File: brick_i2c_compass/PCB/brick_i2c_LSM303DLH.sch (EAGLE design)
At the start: 10 parts, among them J1 BRICK_I2C

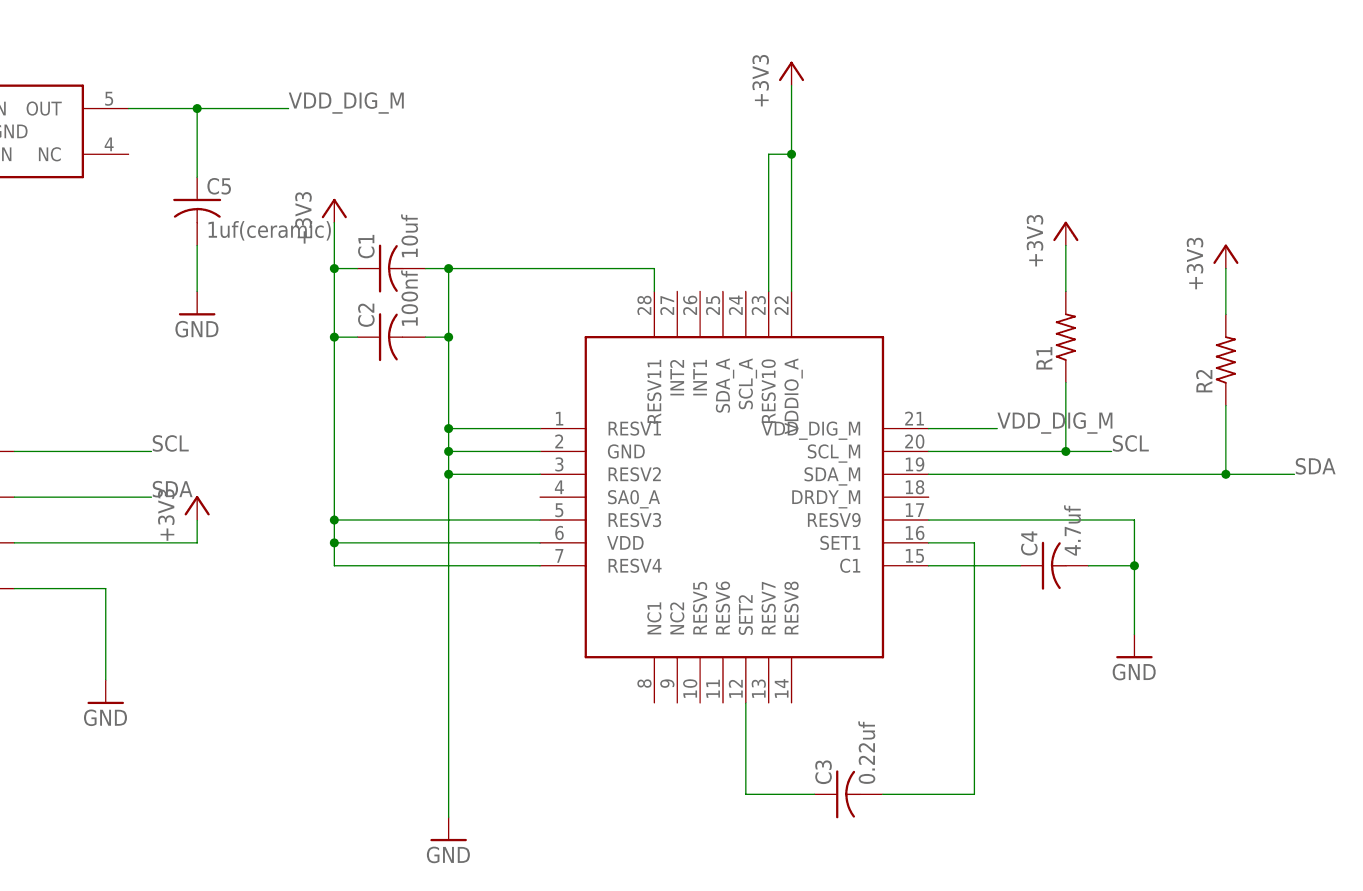
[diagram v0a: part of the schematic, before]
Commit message: Modified for Elecrow
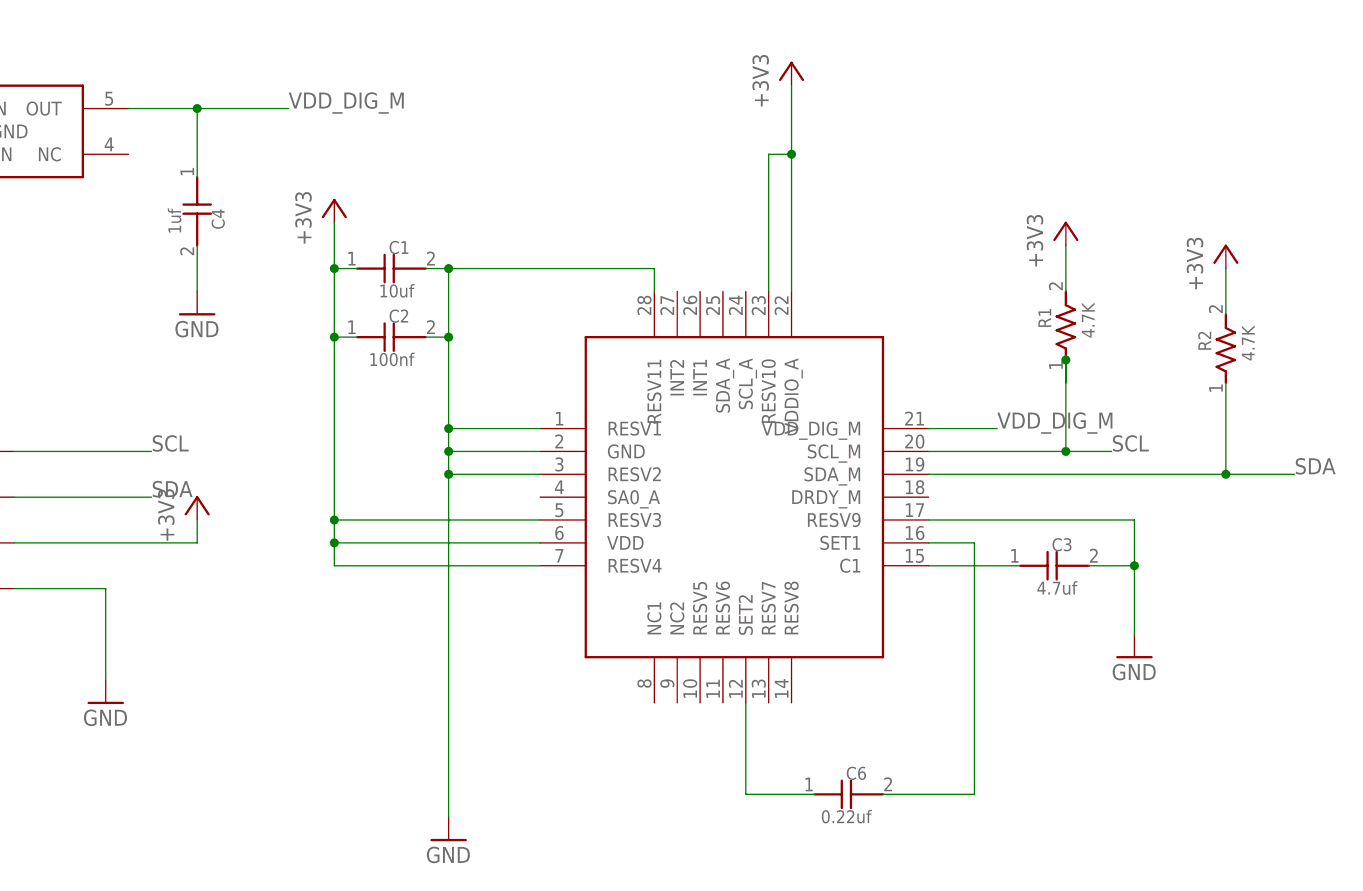
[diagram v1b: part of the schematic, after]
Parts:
- removed C5: 1uf(ceramic), adafruit:C-USC0603
- added C6: 0.22uf, GClue-Capacitor:CAPACITOR0603
- C1, C2: device adafruit:C-USC0603 -> GClue-Capacitor:CAPACITOR0603
- C3: value 0.22uf -> 4.7uf; device adafruit:C-USC0603 -> GClue-Capacitor:CAPACITOR0603
- C4: value 4.7uf -> 1uf; device adafruit:C-USC0603 -> GClue-Capacitor:CAPACITOR0603
- R1, R2: value (none) -> 4.7K; device adafruit:R-US_R0603 -> GClue-Resistors:RESISTOR0603
- U$2: device gclueSensor:ST-LSM303DLH -> GClue-Mems:ST-LSM303DLH
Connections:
- net GND: now also C3.2; no longer C5.2
- net N$1: now also C6.1; no longer C3.1
- net N$2: now also C6.2; no longer C3.2
- net N$3: now also C3.1; no longer C4.1
- net VDD_DIG_M: now also C4.1; no longer C5.1
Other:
- moved on the sheet: R1, R2

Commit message: Update for elecrow
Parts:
- added U$4: (no value), gclue:LOGO_GCLUE-M
- added U$5: (no value), gclue:LOGO_OSHW_T-M
- J1: value BRICK_I2C -> (none)
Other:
- moved on the sheet: J1
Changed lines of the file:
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@@
 <parts>
 <part name="U$1" library="gclue" deviceset="A4L-LOC" device=""/>
-<part name="J1" library="gclue" deviceset="BRICK_I2C" device=""/>
 <part name="GND1" library="supply1" deviceset="GND" device=""/>
 <part name="GND2" library="supply1" deviceset="GND" device=""/>
@@
 <part name="C3" library="GClue-Capacitor" deviceset="CAPACITOR" device="0603" value="4.7uf"/>
 <part name="C4" library="GClue-Capacitor" deviceset="CAPACITOR" device="0603" value="1uf"/>
+<part name="J1" library="gclue" deviceset="BRICK_I2C" device=""/>
+<part name="U$4" library="gclue" deviceset="LOGO_GCLUE" device="-M"/>
+<part name="U$5" library="gclue" deviceset="LOGO_OSHW_T" device="-M"/>
 </parts>
 <sheets>
@@
 <instances>
 <instance part="U$1" gate="G$1" x="0" y="0"/>
-<instance part="J1" gate="G$1" x="40.64" y="63.5"/>
 <instance part="GND1" gate="1" x="58.42" y="43.18"/>
 <instance part="GND2" gate="1" x="96.52" y="27.94"/>
@@
 <instance part="C3" gate="G$1" x="162.56" y="58.42"/>
 <instance part="C4" gate="G$1" x="68.58" y="99.06" rot="R270"/>
+<instance part="J1" gate="G$1" x="35.56" y="63.5"/>
+<instance part="U$4" gate="G$1" x="182.88" y="7.62"/>
+<instance part="U$5" gate="G$1" x="200.66" y="12.7"/>
 </instances>
 <busses>
@@
 <net name="GND" class="0">
 <segment>
-<pinref part="J1" gate="G$1" pin="GND"/>
-<wire x1="48.26" y1="55.88" x2="58.42" y2="55.88" width="0.1524" layer="91"/>
+<wire x1="43.18" y1="55.88" x2="58.42" y2="55.88" width="0.1524" layer="91"/>
 <wire x1="58.42" y1="55.88" x2="58.42" y2="45.72" width="0.1524" layer="91"/>
 <pinref part="GND1" gate="1" pin="GND"/>
+<pinref part="J1" gate="G$1" pin="GND"/>
 </segment>
 <segment>
@@
 <net name="+3V3" class="0">
 <segment>
+<pinref part="+3V1" gate="G$1" pin="+3V3"/>
+<wire x1="43.18" y1="60.96" x2="68.58" y2="60.96" width="0.1524" layer="91"/>
+<wire x1="68.58" y1="60.96" x2="68.58" y2="63.5" width="0.1524" layer="91"/>
 <pinref part="J1" gate="G$1" pin="VCC"/>
-<pinref part="+3V1" gate="G$1" pin="+3V3"/>
-<wire x1="48.26" y1="60.96" x2="68.58" y2="60.96" width="0.1524" layer="91"/>
-<wire x1="68.58" y1="60.96" x2="68.58" y2="63.5" width="0.1524" layer="91"/>
 </segment>
 <segment>
@@
 </segment>
 <segment>
+<wire x1="43.18" y1="66.04" x2="63.5" y2="66.04" width="0.1524" layer="91"/>
+<label x="63.5" y="66.04" size="1.778" layer="95"/>
 <pinref part="J1" gate="G$1" pin="SDA"/>
-<wire x1="48.26" y1="66.04" x2="63.5" y2="66.04" width="0.1524" layer="91"/>
-<label x="63.5" y="66.04" size="1.778" layer="95"/>
 </segment>
 </net>
@@
 </segment>
 <segment>
+<wire x1="43.18" y1="71.12" x2="63.5" y2="71.12" width="0.1524" layer="91"/>
+<label x="63.5" y="71.12" size="1.778" layer="95"/>
 <pinref part="J1" gate="G$1" pin="SCL"/>
-<wire x1="48.26" y1="71.12" x2="63.5" y2="71.12" width="0.1524" layer="91"/>
-<label x="63.5" y="71.12" size="1.778" layer="95"/>
-</segment>
-</net>
+</segment>
+</net>

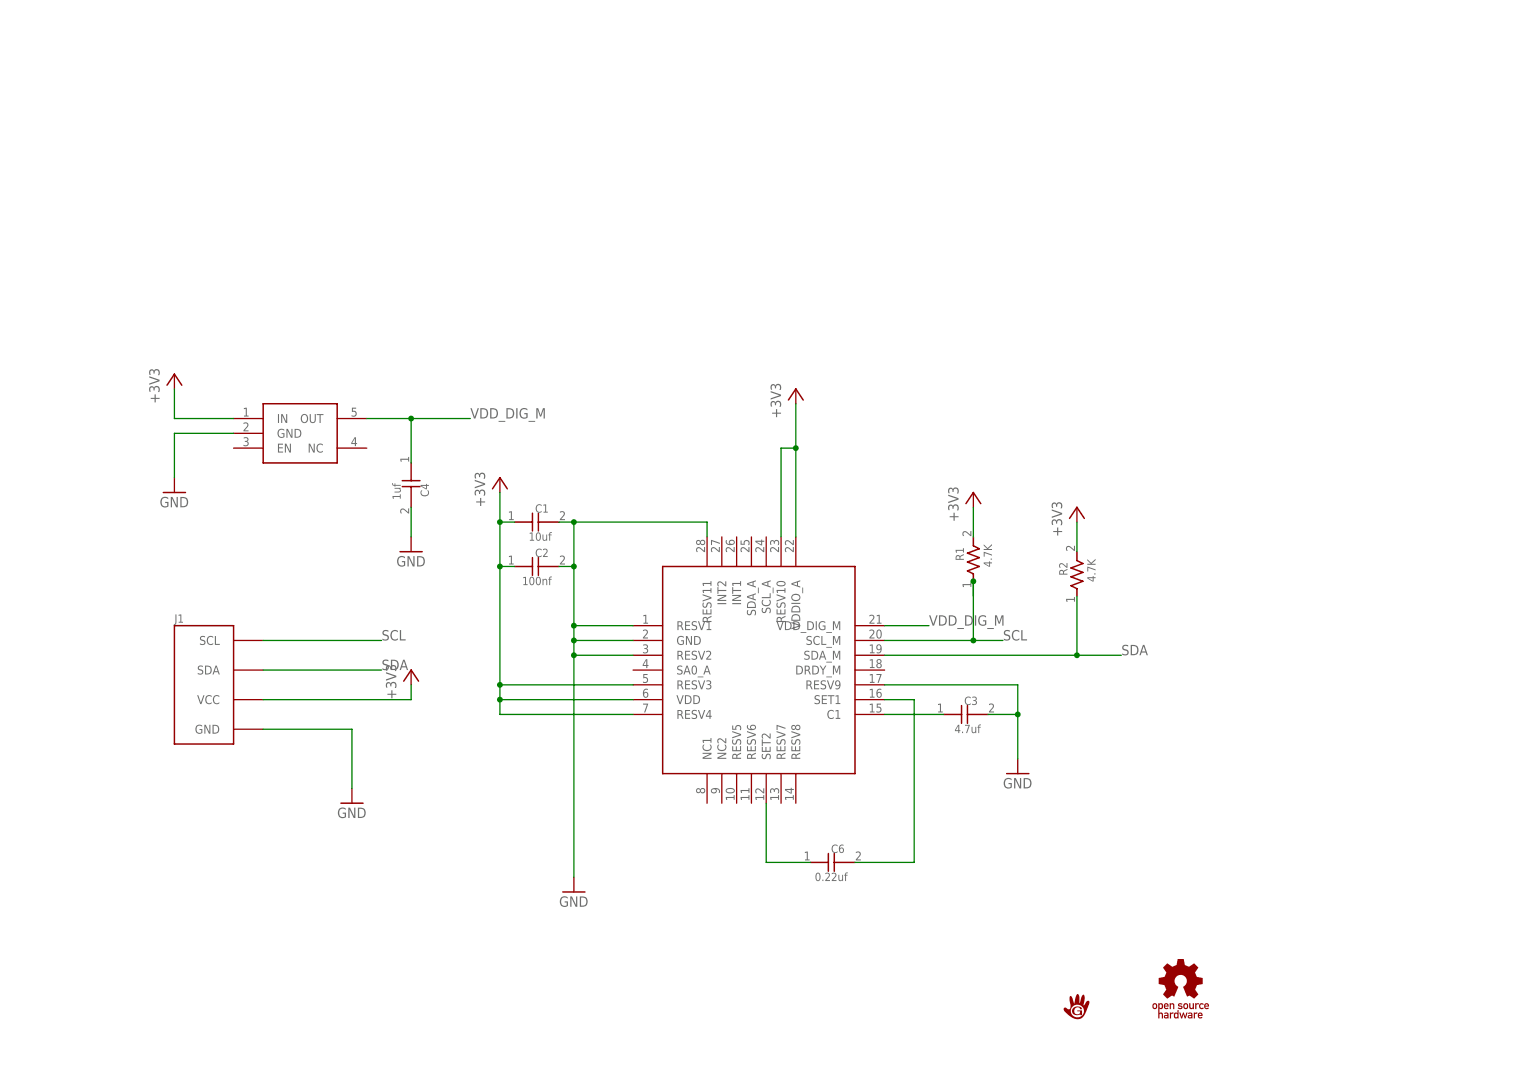
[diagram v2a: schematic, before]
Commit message: refine board size brick_i2c_compass
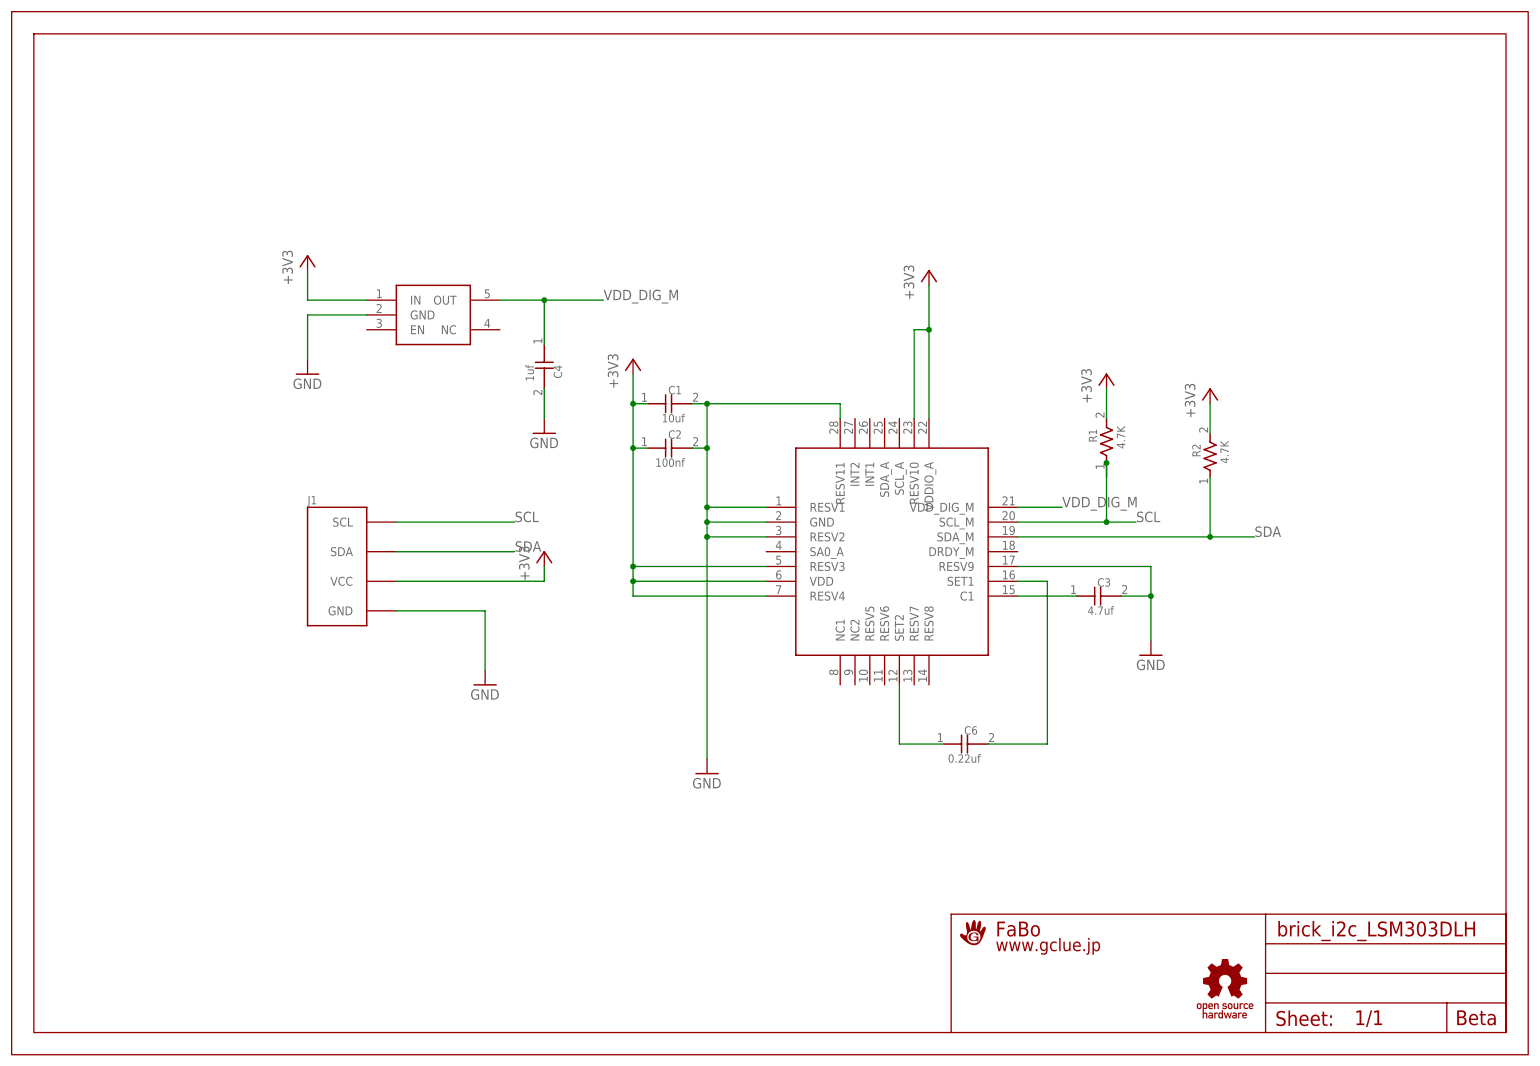
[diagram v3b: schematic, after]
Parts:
- removed U$5: (no value), gclue:LOGO_OSHW_T-M
- added U$1: A4L-LOC-FABO_M, gclue:A4L-LOC-FABO_M
- U$4: device gclue:LOGO_GCLUE-M -> gclue:LOGO_OSHW_T-M
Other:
- note added: "Beta"
- moved on the sheet: C1, C2, C3, C4, C6, J1, R1, R2

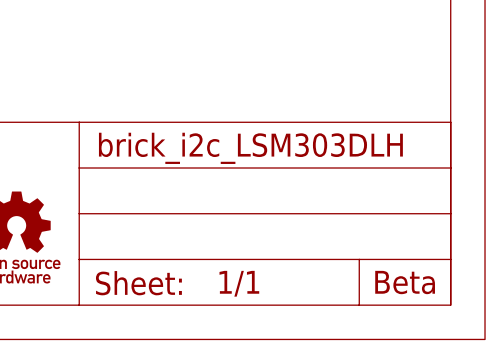
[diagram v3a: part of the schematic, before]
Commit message: change revision number beta->beta2
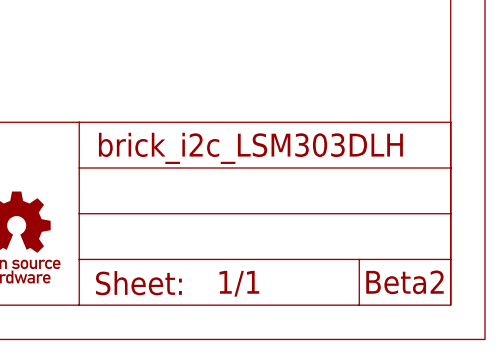
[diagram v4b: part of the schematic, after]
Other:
- note added: "Beta2"
- note removed: "Beta"
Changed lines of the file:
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@@
 <sheet>
 <plain>
-<text x="251.46" y="5.08" size="2.54" layer="94" align="bottom-center">Beta</text>
+<text x="251.46" y="5.08" size="2.54" layer="94" align="bottom-center">Beta2</text>
 </plain>
 <instances>
